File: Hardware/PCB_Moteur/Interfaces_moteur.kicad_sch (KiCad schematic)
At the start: 27 parts, among them J3 Conn_01x02, J7 Conn_02x06_Top_Bottom, U12 MCP1802T-5002I/OT, U2 ISOW1044, U4 LSF0204PWR

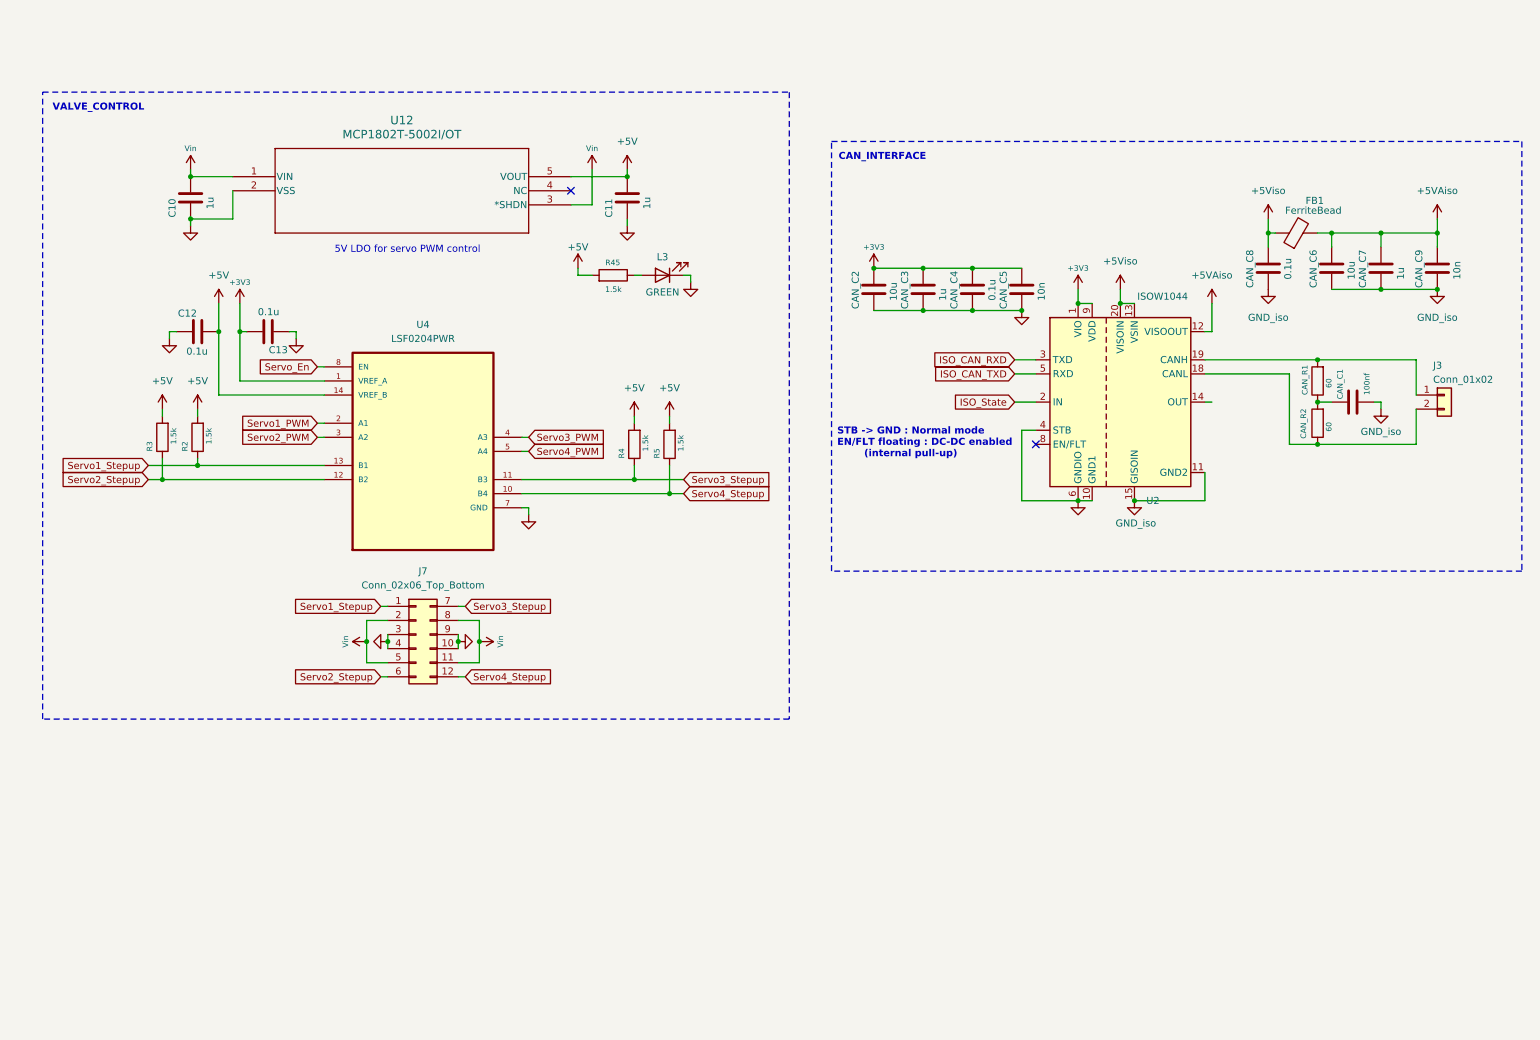
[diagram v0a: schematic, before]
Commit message: fix: LDO SHDN + complete stm32cubeide mapping (kicad missing) + add CAN in binary signal (connector missing)
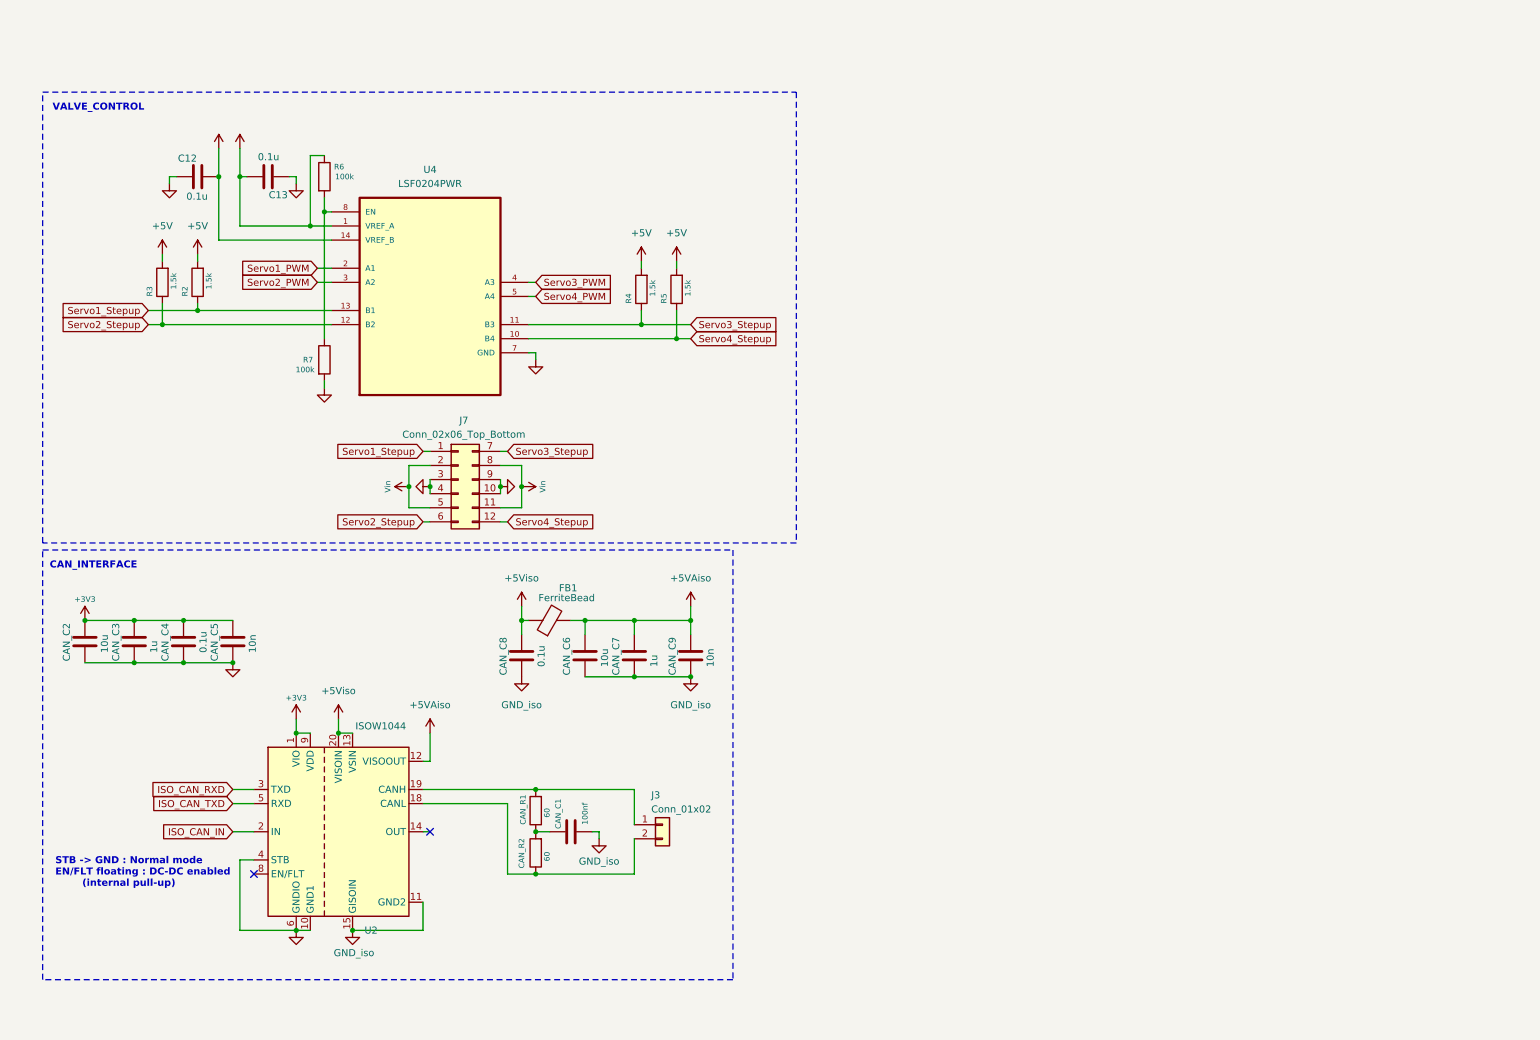
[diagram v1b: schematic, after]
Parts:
- removed C10, C11: 1u, symbol Device:C
- removed L3: GREEN, LED_SMD:LED_0603_1608Metric, symbol Device:LED
- removed R45: 1.5k, Resistor_SMD:R_0603_1608Metric, symbol Device:R
- removed U12: MCP1802T-5002I/OT, SOT-23-5_MC_MCH, symbol 2026-01-14_15-06-07:MCP1802T-5002I_OT
- added R6, R7: 100k, Resistor_SMD:R_0805_2012Metric, symbol Device:R
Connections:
- net +3V3: now also R6.1
- net GND: now also R7.2
- net ISO_State renamed ISO_CAN_IN
- net Servo_En: no longer names the net of U4.8 (EN)
- net Servo_En: now also R6.2, R7.1
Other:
- note removed: "5V LDO for servo PWM control"
- moved on the sheet: C12, C13, CAN_C1, CAN_C2, CAN_C3, CAN_C4, CAN_C5, CAN_C6, CAN_C7, CAN_C8, CAN_C9, CAN_R1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

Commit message: wip : pin mapping on STM32 and limit switch circuit
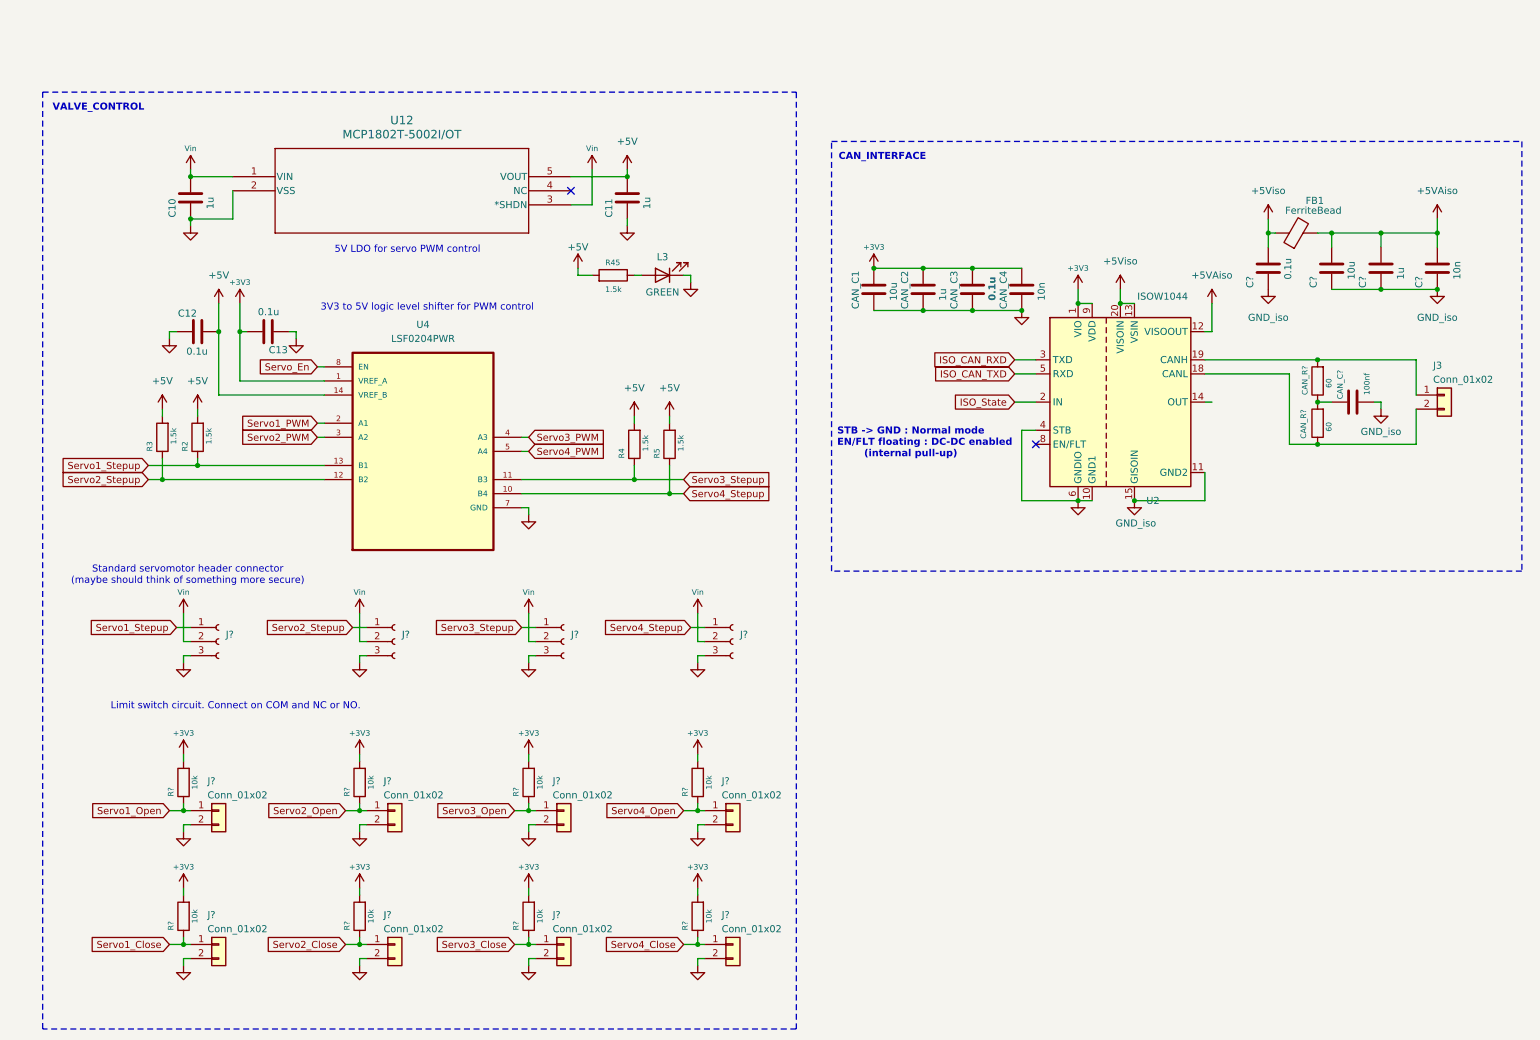
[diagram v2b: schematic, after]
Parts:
- removed J7: Conn_02x06_Top_Bottom, symbol Connector_Generic:Conn_02x06_Top_Bottom
- removed R6, R7: 100k, Resistor_SMD:R_0805_2012Metric, symbol Device:R
- added C10, C11: 1u, symbol Device:C
- added J? (x8): Conn_01x02, symbol Connector_Generic:Conn_01x02
- added J? (x4): Conn_01x03_Socket, Connector_PinHeader_1.00mm:PinHeader_1x03_P1.00mm_Vertical, symbol Connector:Conn_01x03_Socket
- added L3: GREEN, LED_SMD:LED_0603_1608Metric, symbol Device:LED
- added R45: 1.5k, Resistor_SMD:R_0603_1608Metric, symbol Device:R
- added R? (x8): 10k, Resistor_SMD:R_0805_2012Metric, symbol Device:R
- added U12: MCP1802T-5002I/OT, SOT-23-5_MC_MCH, symbol 2026-01-14_15-06-07:MCP1802T-5002I_OT
- renumbered CAN_C9 to C?, CAN_C6 to C?, CAN_C7 to C?, CAN_C8 to C?, CAN_C2 to CAN_C1, CAN_C3 to CAN_C2, CAN_C4 to CAN_C3, CAN_C5 to CAN_C4, CAN_C1 to CAN_C?, CAN_R2 to CAN_R?, CAN_R1 to CAN_R?
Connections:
- net +3V3: now also R?.2, R?.2, R?.2, R?.2, R?.2, R?.2, R?.2, R?.2
- net +5V: now also C11.1, R45.2, U12.5 (VOUT)
- net GND: now also C10.2, C11.2, J?.2 (Pin_2), J?.2 (Pin_2), J?.2 (Pin_2), J?.2 (Pin_2), J?.2 (Pin_2), J?.2 (Pin_2), J?.2 (Pin_2), J?.2 (Pin_2), J?.3 (Pin_3), J?.3 (Pin_3), J?.3 (Pin_3), J?.3 (Pin_3), L3.1 (K), U12.2 (VSS)
- net Servo1_Stepup: now also J?.1 (Pin_1)
- net Servo2_Stepup: now also J?.1 (Pin_1)
- net Servo3_Stepup: now also J?.1 (Pin_1)
- net Servo4_Stepup: now also J?.1 (Pin_1)
- net Vin: now also C10.1, J?.2 (Pin_2), J?.2 (Pin_2), J?.2 (Pin_2), J?.2 (Pin_2), U12.1 (VIN), U12.3 (*SHDN)
- net Servo_En: now reaches U4.8 (EN)
- net ISO_CAN_IN renamed ISO_State
- new net: L3.2 (A), R45.1
- new net Servo1_Close: J?.1 (Pin_1), R?.1
- new net Servo1_Open: J?.1 (Pin_1), R?.1
- new net Servo2_Close: J?.1 (Pin_1), R?.1
- new net Servo2_Open: J?.1 (Pin_1), R?.1
- new net Servo3_Close: J?.1 (Pin_1), R?.1
- new net Servo3_Open: J?.1 (Pin_1), R?.1
- new net Servo4_Close: J?.1 (Pin_1), R?.1
- new net Servo4_Open: J?.1 (Pin_1), R?.1
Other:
- note added: "3V3 to 5V logic level shifter for PWM control"
- note added: "5V LDO for servo PWM control"
- note added: "Limit switch circuit. Connect on COM and NC or NO."
- note added: "Standard servomotor header connector (maybe should think of something more secure)"
- moved on the sheet: C12, C13, C?, CAN_C1, CAN_C2, CAN_C3, CAN_C4, CAN_C?, CAN_R?, FB1, J3, R2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

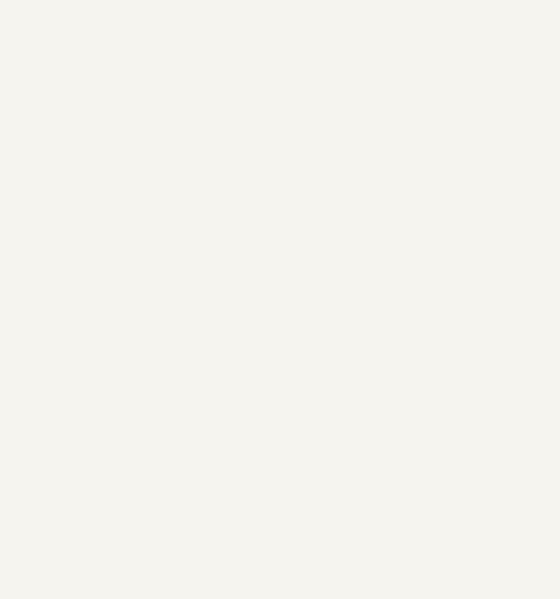
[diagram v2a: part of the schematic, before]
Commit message: feat: add extend ios + fix mapping kicad + add transmitter resistors
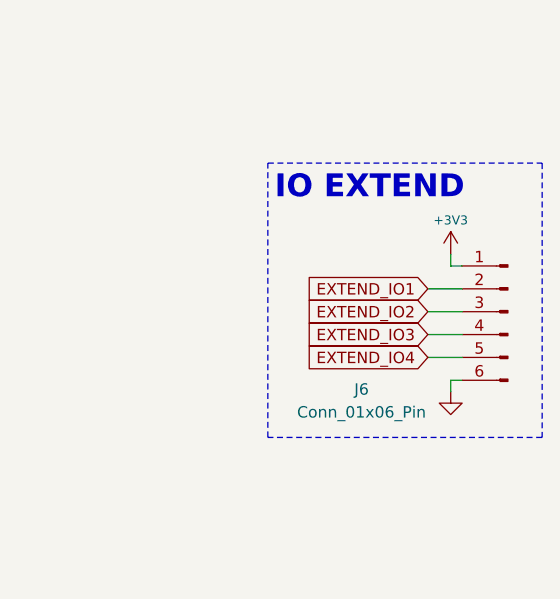
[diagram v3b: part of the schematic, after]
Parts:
- added J6: Conn_01x06_Pin, symbol Connector:Conn_01x06_Pin
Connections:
- net +3V3: now also J6.1 (Pin_1)
- net GND: now also J6.6 (Pin_6)
- new net EXTEND_IO1: J6.2 (Pin_2)
- new net EXTEND_IO2: J6.3 (Pin_3)
- new net EXTEND_IO3: J6.4 (Pin_4)
- new net EXTEND_IO4: J6.5 (Pin_5)
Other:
- note added: "IO EXTEND"
